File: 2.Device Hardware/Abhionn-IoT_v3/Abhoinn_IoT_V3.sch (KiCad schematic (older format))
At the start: 41 parts, among them J1 Conn_01x02, J2 Conn_01x02, J3 Conn_02x05_Odd_Even, J4 Conn_02x05_Odd_Even, J5 Conn_Coaxial, J6 Conn_01x02_Female, U1 XC6206PxxxMR, U3 STM32L082KZTx

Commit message: Update Drawing
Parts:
- added IC?: AX-SIP-SFEU-1-01-TX30, AXSIPSFEU101TX30, symbol SamacSys_Parts:AX-SIP-SFEU-1-01-TX30
- added IC?: MS5840-02BA01, MS584002BA01, symbol SamacSys_Parts:MS5840-02BA01
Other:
- note removed: "USB \n"
- moved on the sheet: D4, JP1, JP2, JP3, JP4, R1, R4, U3

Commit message: Final Rev layout, Add build Files
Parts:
- IC1: renamed from IC?; symbol SamacSys_Parts:AX-SIP-SFEU-1-01-TX30 -> Abhoinn_IoT_V3-rescue:AX-SIP-SFEU-1-01-TX30-SamacSys_Parts
- IC2: renamed from IC?; symbol SamacSys_Parts:MS5840-02BA01 -> Abhoinn_IoT_V3-rescue:MS5840-02BA01-SamacSys_Parts
- U3: value STM32L082KZTx -> STM32L071RBTx; LCSC Part # (none) -> C115942
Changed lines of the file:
@@
 P 2050 3600
 F 0 "U3" H 2400 2500 50  0000 C CNN
-F 1 "STM32L082KZTx" H 2400 2600 50  0000 C CNN
+F 1 "STM32L071RBTx" H 2400 2600 50  0000 C CNN
 F 2 "Package_QFP:LQFP-32_7x7mm_P0.8mm" H 1550 2700 50  0001 R CNN
 F 3 "http://www.st.com/st-web-ui/static/active/en/resource/technical/document/datasheet/DM00141132.pdf" H 2050 3600 50  0001 C CNN
+F 4 "C115942" H 2050 3600 50  0001 C CNN "LCSC Part #"
 	1    2050 3600
 	1    0    0    -1
@@
 $EndComp
 $Comp
-L SamacSys_Parts:AX-SIP-SFEU-1-01-TX30 IC?
+L Abhoinn_IoT_V3-rescue:AX-SIP-SFEU-1-01-TX30-SamacSys_Parts IC1
 U 1 1 6115E19D
 P 6400 6200
-F 0 "IC?" H 7550 6465 50  0000 C CNN
+F 0 "IC1" H 7550 6465 50  0000 C CNN
 F 1 "AX-SIP-SFEU-1-01-TX30" H 7550 6374 50  0000 C CNN
 F 2 "AXSIPSFEU101TX30" H 8550 6300 50  0001 L CNN
@@
 $EndComp
 $Comp
-L SamacSys_Parts:MS5840-02BA01 IC?
+L Abhoinn_IoT_V3-rescue:MS5840-02BA01-SamacSys_Parts IC2
 U 1 1 61162190
 P 11100 6400
-F 0 "IC?" H 11650 6665 50  0000 C CNN
+F 0 "IC2" H 11650 6665 50  0000 C CNN
 F 1 "MS5840-02BA01" H 11650 6574 50  0000 C CNN
 F 2 "MS584002BA01" H 12050 6500 50  0001 L CNN

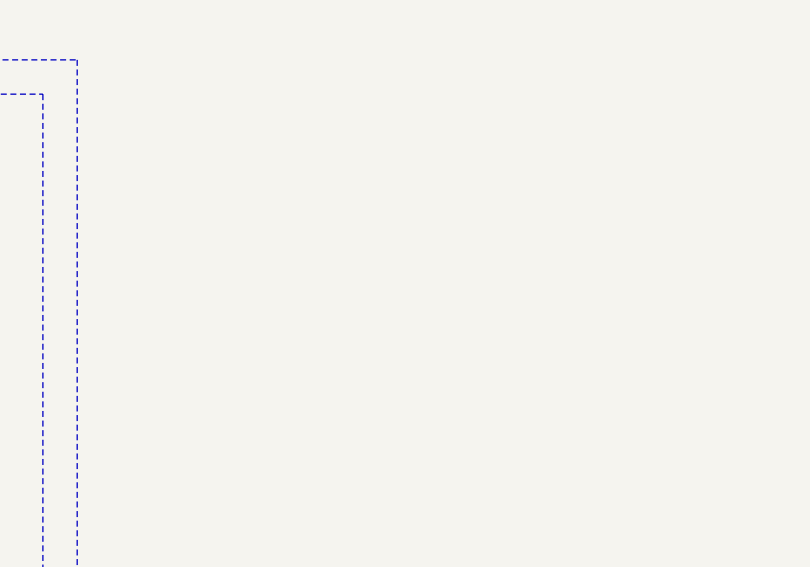
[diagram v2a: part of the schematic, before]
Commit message: Add layout for 48 pin MCU
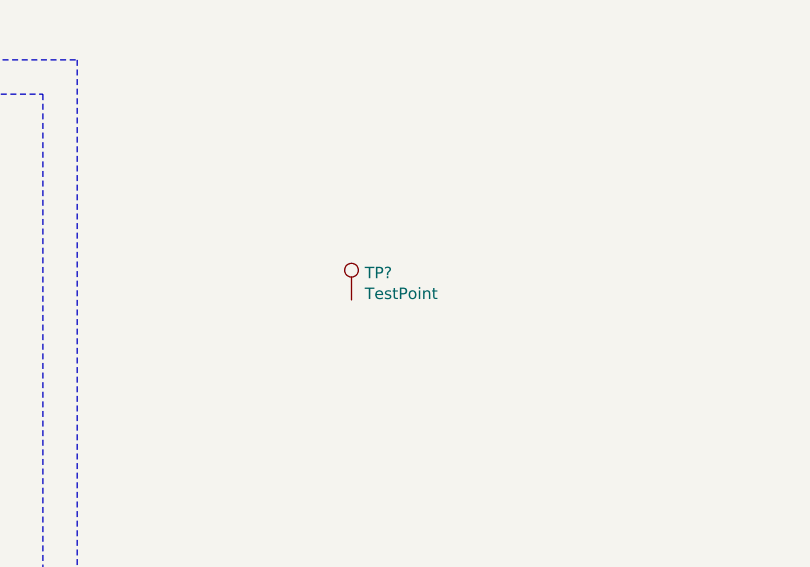
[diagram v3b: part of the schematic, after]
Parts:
- added TP?: TestPoint, symbol Connector:TestPoint
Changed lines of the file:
@@
+	1    0    0    -1
+$EndComp
+$Comp
+L Connector:TestPoint TP?
+U 1 1 6136B227
+P 10650 3450
+F 0 "TP?" H 10708 3568 50  0000 L CNN
+F 1 "TestPoint" H 10708 3477 50  0000 L CNN
+F 2 "" H 10850 3450 50  0001 C CNN
+F 3 "~" H 10850 3450 50  0001 C CNN
+	1    10650 3450
 	1    0    0    -1
 $EndComp
